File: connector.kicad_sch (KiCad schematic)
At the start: 2 parts, among them J401 AXK500137YG, J402 AXK500137YG

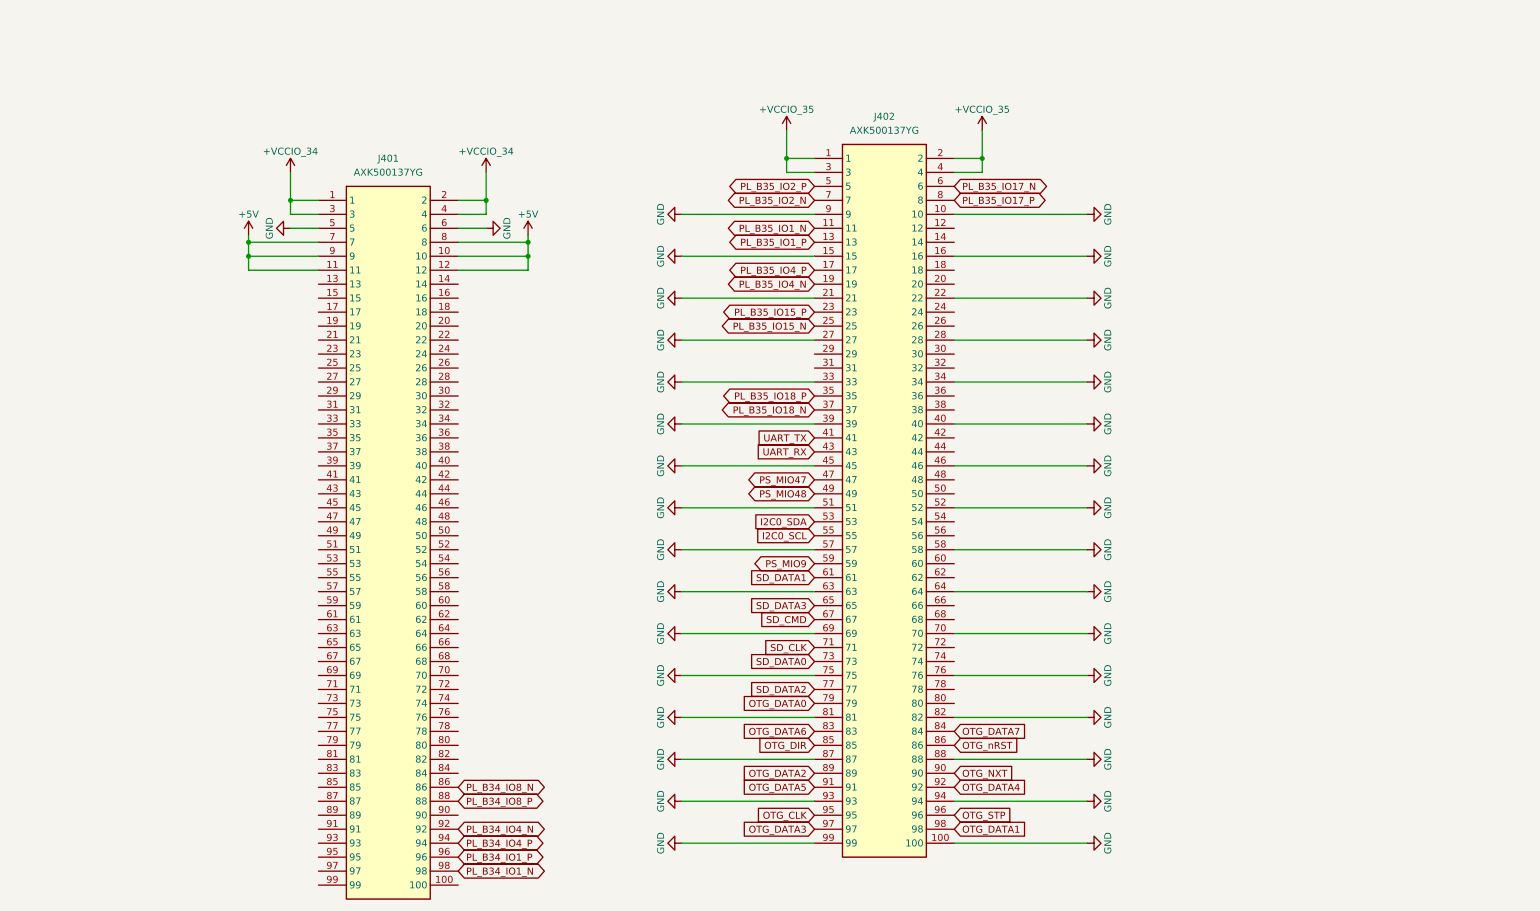
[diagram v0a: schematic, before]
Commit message: layout: routing bank 34
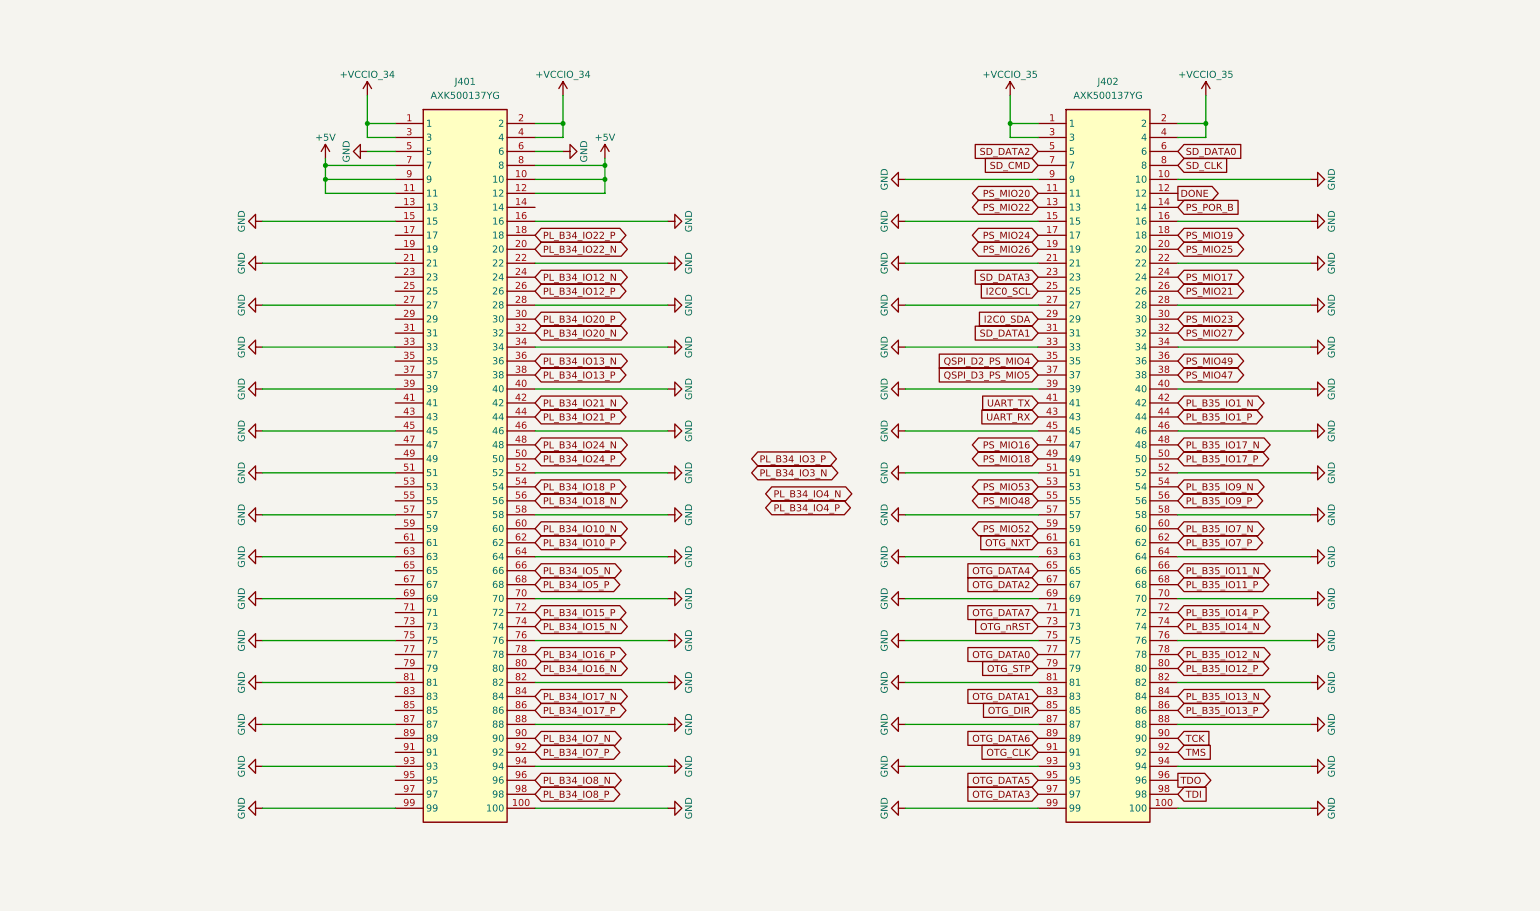
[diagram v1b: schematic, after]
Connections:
- net PL_B34_IO1_N is gone; now on net PL_B34_IO8_P: J401.98
- net PL_B34_IO1_P is gone; now on net PL_B34_IO8_N: J401.96
- net PL_B35_IO15_N is gone; now on net I2C0_SCL: J402.25
- net PL_B35_IO15_P is gone; now on net SD_DATA3: J402.23
- net PL_B35_IO2_N is gone; now on net SD_CMD: J402.7
- net PL_B35_IO2_P is gone; now on net SD_DATA2: J402.5
- net GND: now also J401.100, J401.15, J401.16, J401.21, J401.22, J401.27, J401.28, J401.33, J401.34, J401.39, J401.40, J401.45, J401.46, J401.51, J401.52, J401.57, J401.58, J401.63, J401.64, J401.69, J401.70, J401.75, J401.76, J401.81, J401.82, J401.87, J401.88, J401.93, J401.94, J401.99
- net I2C0_SCL: no longer J402.55
- net I2C0_SDA: now also J402.29; no longer J402.53
- net OTG_CLK: now also J402.91; no longer J402.95
- net OTG_DATA0: now also J402.77; no longer J402.79
- net OTG_DATA1: now also J402.83; no longer J402.98
- net OTG_DATA2: now also J402.67; no longer J402.89
- net OTG_DATA4: now also J402.65; no longer J402.92
- net OTG_DATA5: now also J402.95; no longer J402.91
- net OTG_DATA6: now also J402.89; no longer J402.83
- net OTG_DATA7: now also J402.71; no longer J402.84
- net OTG_NXT: now also J402.61; no longer J402.90
- net OTG_STP: now also J402.79; no longer J402.96
- net OTG_nRST: now also J402.73; no longer J402.86
- net PL_B34_IO4_N: no longer J401.92
- net PL_B34_IO4_P: no longer J401.94
- net PL_B34_IO8_N: no longer J401.86
- net PL_B34_IO8_P: no longer J401.88
- net PL_B35_IO17_N: now also J402.48; no longer J402.6
- net PL_B35_IO17_P: now also J402.50; no longer J402.8
- net PL_B35_IO1_N: now also J402.42; no longer J402.11
- net PL_B35_IO1_P: now also J402.44; no longer J402.13
- net PS_MIO47: now also J402.38; no longer J402.47
- net PS_MIO48: now also J402.55; no longer J402.49
- net SD_CLK: now also J402.8; no longer J402.71
- net SD_CMD: no longer J402.67
- net SD_DATA0: now also J402.6; no longer J402.73
- net SD_DATA1: now also J402.31; no longer J402.61
- net SD_DATA2: no longer J402.77
- net SD_DATA3: no longer J402.65
- net DONE: now reaches J402.12
- net PS_POR_B: now reaches J402.14
- net PS_MIO19: now reaches J402.18
- net PS_MIO25: now reaches J402.20
- net PS_MIO17: now reaches J402.24
- net PS_MIO21: now reaches J402.26
- net PS_MIO23: now reaches J402.30
- net PS_MIO27: now reaches J402.32
- net PS_MIO49: now reaches J402.36
- net PL_B35_IO9_N: now reaches J402.54
- net PL_B35_IO9_P: now reaches J402.56
- net PL_B35_IO7_N: now reaches J402.60
- net PL_B35_IO7_P: now reaches J402.62
- net PL_B35_IO11_N: now reaches J402.66
- net PL_B35_IO11_P: now reaches J402.68
- net PL_B35_IO14_P: now reaches J402.72
- net PL_B35_IO14_N: now reaches J402.74
- net PL_B35_IO12_N: now reaches J402.78
- net PL_B35_IO12_P: now reaches J402.80
- net PL_B34_IO22_P: now reaches J401.18
- net PL_B34_IO22_N: now reaches J401.20
- net PL_B34_IO12_N: now reaches J401.24
- net PL_B34_IO12_P: now reaches J401.26
- net PL_B34_IO20_P: now reaches J401.30
- net PL_B34_IO20_N: now reaches J401.32
- net PL_B34_IO13_N: now reaches J401.36
- net PL_B34_IO13_P: now reaches J401.38
- net PL_B34_IO21_N: now reaches J401.42
- net PL_B34_IO21_P: now reaches J401.44
- net PL_B34_IO24_N: now reaches J401.48
- net PL_B34_IO24_P: now reaches J401.50
- net PL_B34_IO18_P: now reaches J401.54
- net PL_B34_IO18_N: now reaches J401.56
- net PL_B34_IO10_N: now reaches J401.60
- net PL_B34_IO10_P: now reaches J401.62
- net PL_B34_IO5_N: now reaches J401.66
- net PL_B34_IO5_P: now reaches J401.68
- net PL_B34_IO15_P: now reaches J401.72
- net PL_B34_IO15_N: now reaches J401.74
- net PL_B34_IO16_P: now reaches J401.78
- net PL_B34_IO16_N: now reaches J401.80
- net PL_B34_IO17_N: now reaches J401.84
- net PL_B34_IO7_N: now reaches J401.90
- net PL_B35_IO18_N renamed QSPI_D3_PS_MIO5
- net PL_B35_IO18_P renamed QSPI_D2_PS_MIO4
- net PL_B35_IO4_N renamed PS_MIO26
- net PL_B35_IO4_P renamed PS_MIO24
- net PS_MIO9 renamed PS_MIO52
- new net PL_B34_IO17_P: J401.86
- new net PL_B34_IO7_P: J401.92
- new net PL_B35_IO13_N: J402.84
- new net PL_B35_IO13_P: J402.86
- new net PS_MIO16: J402.47
- new net PS_MIO18: J402.49
- new net PS_MIO20: J402.11
- new net PS_MIO22: J402.13
- new net PS_MIO53: J402.53
- new net TCK: J402.90
- new net TDI: J402.98
- new net TDO: J402.96
- new net TMS: J402.92
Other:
- moved on the sheet: J401, J402

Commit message: layout: before rerouting ddr
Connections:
- net PL_B34_IO10_N: now also J401.62; no longer J401.60
- net PL_B34_IO10_P: now also J401.60; no longer J401.62
- net PL_B34_IO13_N: now also J401.38; no longer J401.36
- net PL_B34_IO13_P: now also J401.36; no longer J401.38
- net PL_B34_IO3_N: now also J401.83
- net PL_B34_IO3_P: now also J401.85
- net PL_B34_IO4_N: now also J401.61
- net PL_B34_IO4_P: now also J401.59
- net PL_B34_IO8_N: now also J401.98; no longer J401.96
- net PL_B34_IO8_P: now also J401.96; no longer J401.98
- net PL_B34_IO23_N: now reaches J401.47
- net PL_B34_IO25: now reaches J401.49
- net PL_B34_IO0: now reaches J401.53
- net PL_B34_IO23_P: now reaches J401.55
- net PL_B34_IO14_P: now reaches J401.65
- net PL_B34_IO14_N: now reaches J401.67
- net PL_B34_IO9_N: now reaches J401.71
- net PL_B34_IO9_P: now reaches J401.73
- net PL_B34_IO11_P: now reaches J401.77
- net PL_B34_IO11_N: now reaches J401.79
- net PL_B34_IO2_N: now reaches J401.89
- net PL_B34_IO2_P: now reaches J401.91
- net PL_B34_IO1_P: now reaches J401.95
- net PL_B34_IO1_N: now reaches J401.97
- net PL_B34_IO24_N renamed PL_B34_IO19_N
- net PL_B34_IO24_P renamed PL_B34_IO19_P
- no-connect marks 0 -> 12
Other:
- note added: "Reserved for Bank 13"
